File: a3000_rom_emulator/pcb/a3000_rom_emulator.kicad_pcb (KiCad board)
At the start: 4 copper layers, 43.2 x 78.7 mm, 92 parts

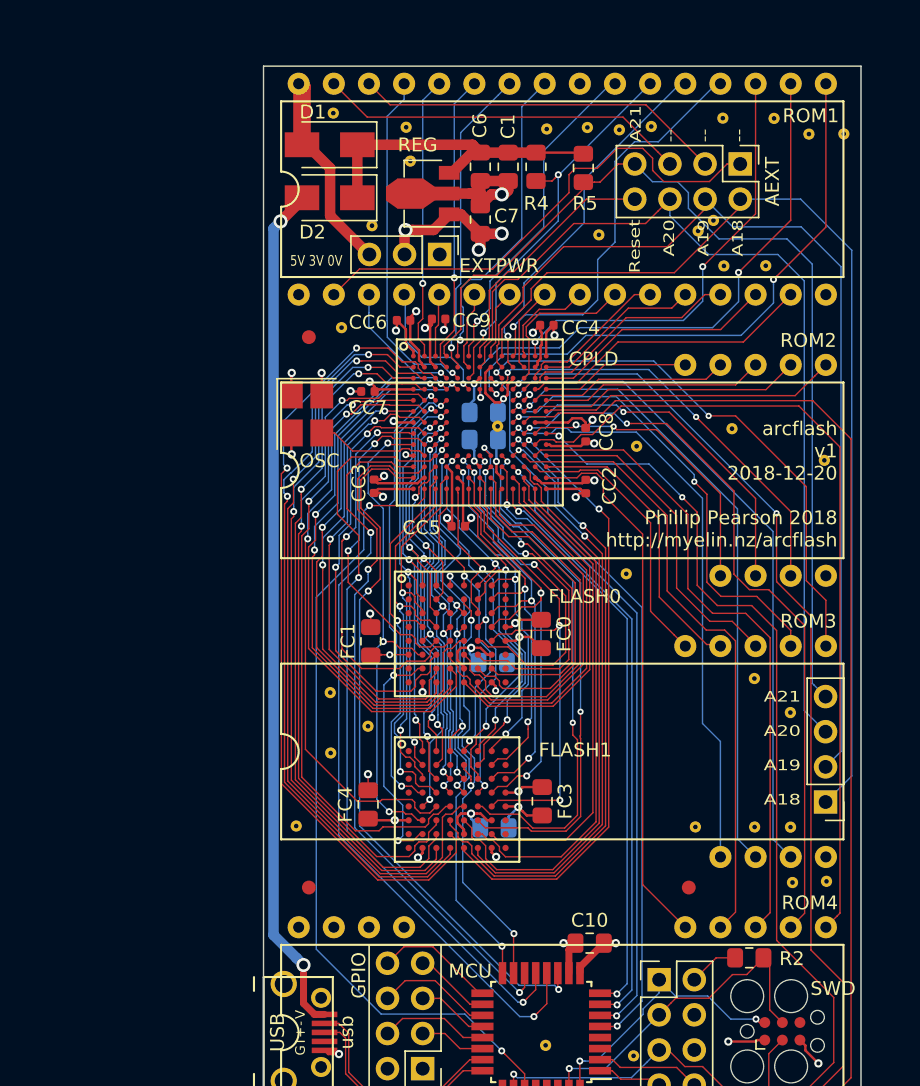
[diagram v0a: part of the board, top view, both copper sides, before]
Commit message: Starting on v2: renamed arc_RESET pin to rom_nOE and added jumper to connect LA21 to rom_A19
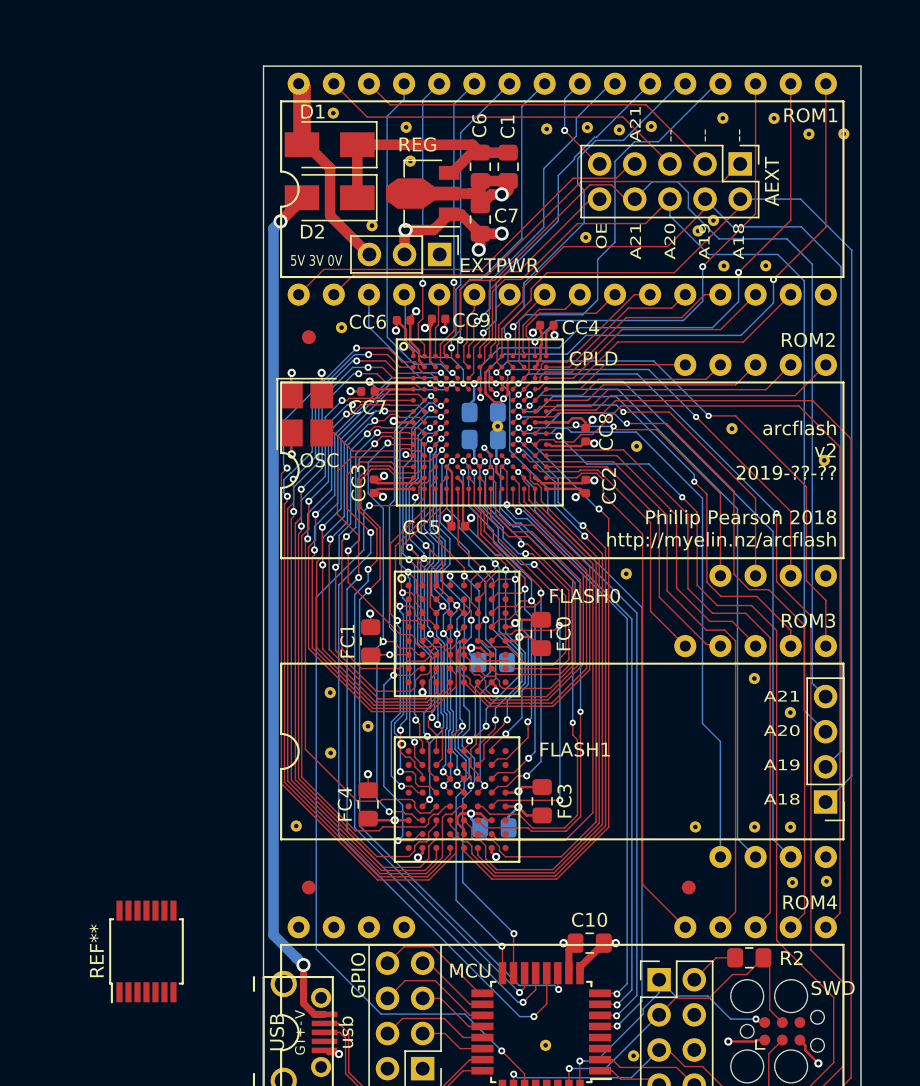
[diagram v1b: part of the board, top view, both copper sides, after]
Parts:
- removed the AEXT at (174.2, 36.3)
- removed R4, R5: 10k, Resistor_SMD:R_0805_2012Metric_Pad1.15x1.40mm_HandSolder
- added AEXT: Extras, Connector_PinHeader_2.54mm:PinHeader_2x05_P2.54mm_Vertical, F.Cu at (174.2, 36.3)
- added REF**: TSSOP-14_4.4x5mm_P0.65mm, Package_SO:TSSOP-14_4.4x5mm_P0.65mm, F.Cu at (131.2, 93.2)
- moved staple_single19 0.97 mm to (163.0, 41.6)
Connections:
- CPLD pad A7: arc_RESET -> rom_nOE
- ROM1 pad 1: (no net) -> rom_A19_ext
- ROM1 pad 24: (no net) -> rom_nOE_ext
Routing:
- net rom_A19_ext: track 0.00 -> 28.2 mm
- net arc_RESET: track 18.3 -> 0.00 mm
- net rom_nOE: track 0.00 -> 15.7 mm
- net rom_nOE_ext: track 0.00 -> 7.37 mm, vias 0 -> 1
- net 5V: track 23.3 -> 17.8 mm
- net rom_A16_ext: track 36.6 -> 33.3 mm
- net rom_nCS: track 28.5 -> 26.8 mm, vias 2 -> 1
- net rom_D7: track 26.4 -> 27.9 mm
- net flash_A19: track 29.2 -> 28.6 mm
- net rom_A19: track 70.2 -> 69.6 mm
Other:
- board text added: "OE A21 A20 A19 A18"
- board text added: "TODO - wire up A21 (rom_A19) to ROM pin 1 - remove pullups for A21 and romcs* - remove osc and add pin + gnd - add power sense voltage divider -> mcu gpio - OR 74lvt125d for: - reset sense - reset drive - power sense - POR drive -> then we can use the CPLD reset pin for RPC OE"
- board text added: "arcflash v2 2019-??-?? Phillip Pearson 2018 http://myelin.nz/arcflash"
- board text removed: "Reset A20 A19 A18"
- board text removed: "arcflash v1 2018-12-20 Phillip Pearson 2018 http://myelin.nz/arcflash"

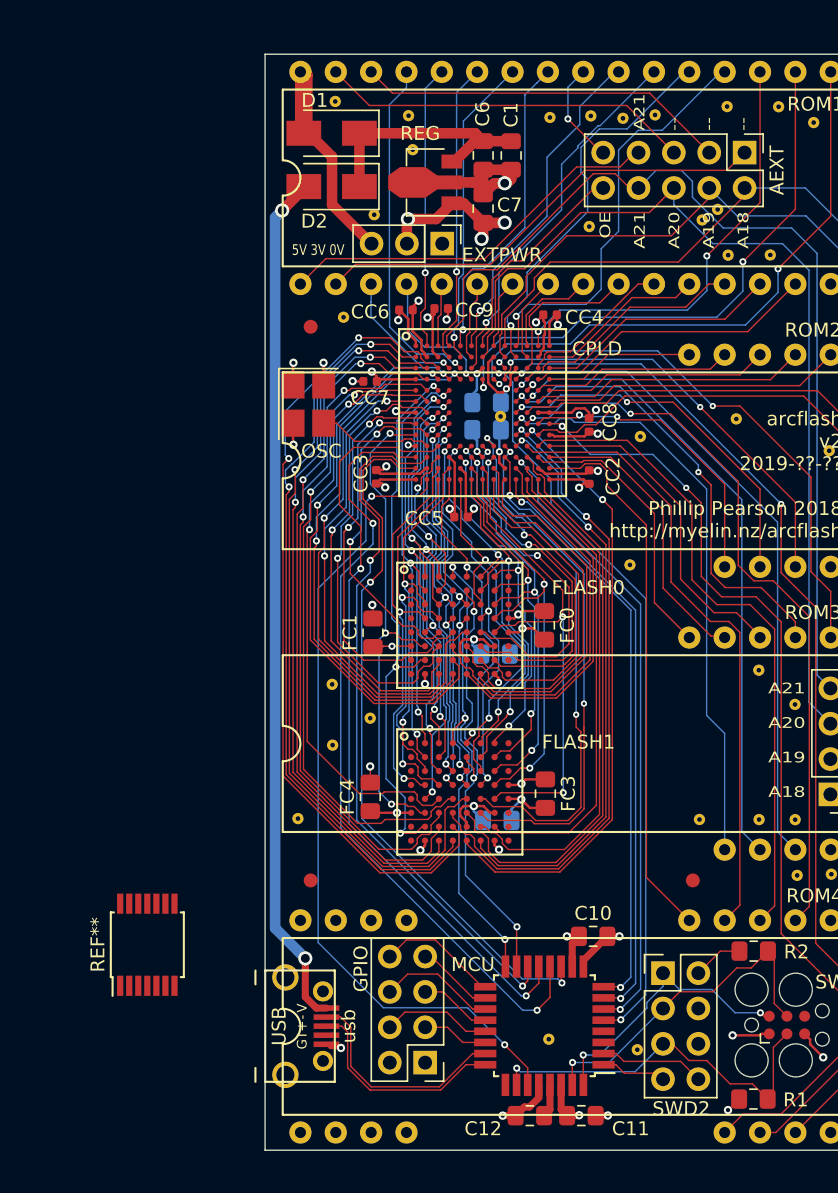
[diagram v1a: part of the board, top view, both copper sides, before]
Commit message: v2: 74lvt125 added and all lines routed, I think
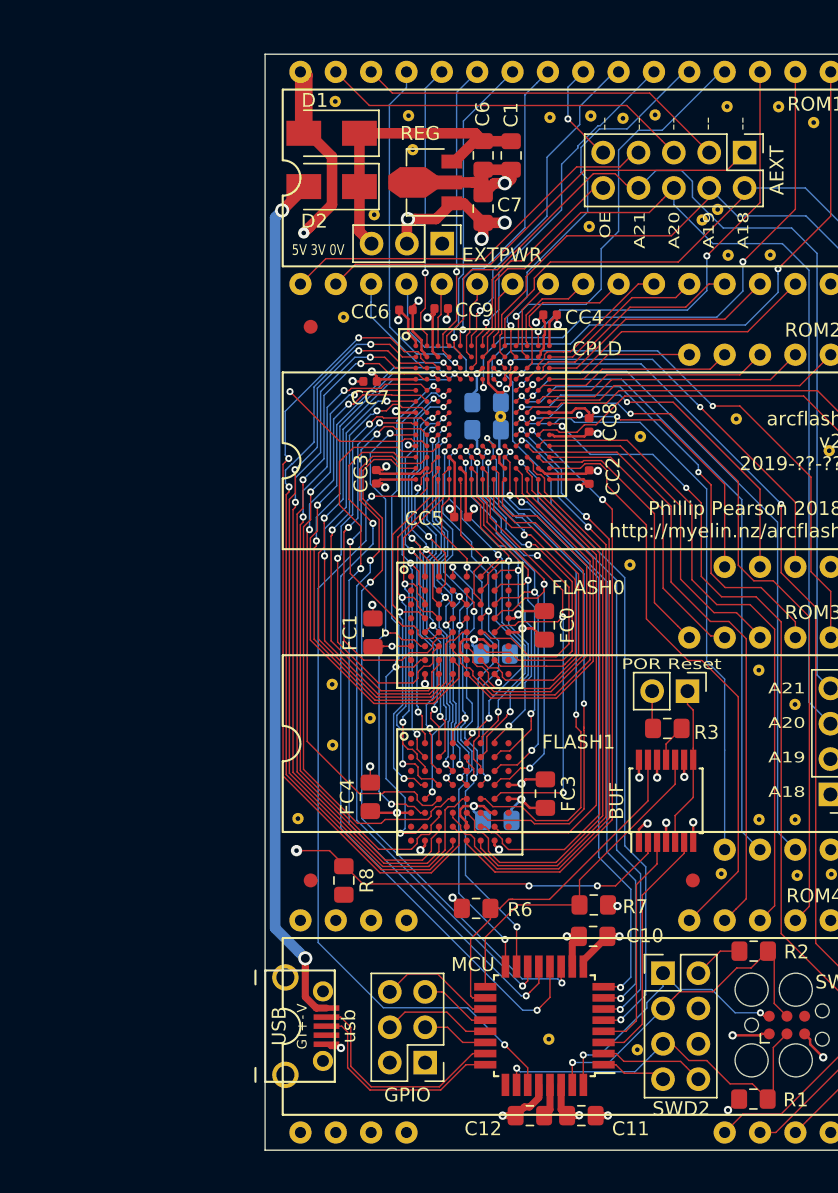
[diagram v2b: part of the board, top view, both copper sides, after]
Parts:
- removed the GPIO at (151.2, 101.7)
- removed OSC: osc, Oscillator:Oscillator_SMD_Abracon_ASE-4Pin_3.2x2.5mm_HandSoldering
- removed REF**: TSSOP-14_4.4x5mm_P0.65mm, Package_SO:TSSOP-14_4.4x5mm_P0.65mm
- added BUF: Reset buffer, Package_SO:TSSOP-14_4.4x5mm_P0.65mm, F.Cu at (168.5, 82.8)
- added GPIO: gpio, Connector_PinHeader_2.54mm:PinHeader_2x03_P2.54mm_Vertical, F.Cu at (151.2, 101.7)
- added R3: 100R, Resistor_SMD:R_0805_2012Metric_Pad1.15x1.40mm_HandSolder, F.Cu at (168.6, 77.7)
- added R6: NF 10k, Resistor_SMD:R_0805_2012Metric_Pad1.15x1.40mm_HandSolder, F.Cu at (154.9, 90.6)
- added R7: NF 10k, Resistor_SMD:R_0805_2012Metric_Pad1.15x1.40mm_HandSolder, F.Cu at (163.3, 90.3)
- added R8: 10k, Resistor_SMD:R_0805_2012Metric_Pad1.15x1.40mm_HandSolder, F.Cu at (145.4, 88.6)
- added RESET: reset/POR, Connector_PinHeader_2.54mm:PinHeader_1x02_P2.54mm_Vertical, F.Cu at (170.1, 75.0)
- moved staple_single30 4.20 mm to (172.5, 88.1)
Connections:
- CPLD pad K2: cpld_clock_osc -> rom_5V
- EXTPWR pad 3: rom_5V -> 5V
- MCU pad 17: mcu_GPIO5 -> ndrive_arc_RESET
- MCU pad 18: mcu_GPIO4 -> ndrive_arc_POR
- MCU pad 3: (no net) -> arc_RESET_buffered
- MCU pad 4: (no net) -> rom_5V_buffered
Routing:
- net rom_5V: track 14.7 -> 100.2 mm, vias 0 -> 5
- net ndrive_arc_POR: track 0.00 -> 25.6 mm
- net ndrive_arc_RESET: track 0.00 -> 24.6 mm
- net arc_RESET_buffered: track 0.00 -> 17.7 mm
- net rom_5V_buffered: track 0.00 -> 16.1 mm
- net arc_RESET: track 0.00 -> 11.5 mm
- net mcu_GPIO5: track 8.74 -> 0.00 mm
- net cpld_clock_osc: track 8.24 -> 0.00 mm
- net mcu_GPIO4: track 5.55 -> 0.00 mm
- net GND: track 80.6 -> 86.0 mm, vias 28 -> 32
- net 5V: track 17.8 -> 22.3 mm
- net rom_D31: track 39.2 -> 42.7 mm
- net arc_POR_R: track 0.00 -> 2.71 mm
- net arc_POR: track 0.00 -> 2.71 mm
- net 3V3: track 87.4 -> 87.3 mm, vias 25 -> 26
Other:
- board text added: "-- -- -- -- --"
- board text added: "POR Reset"
- board text removed: "A21 -- -- --"

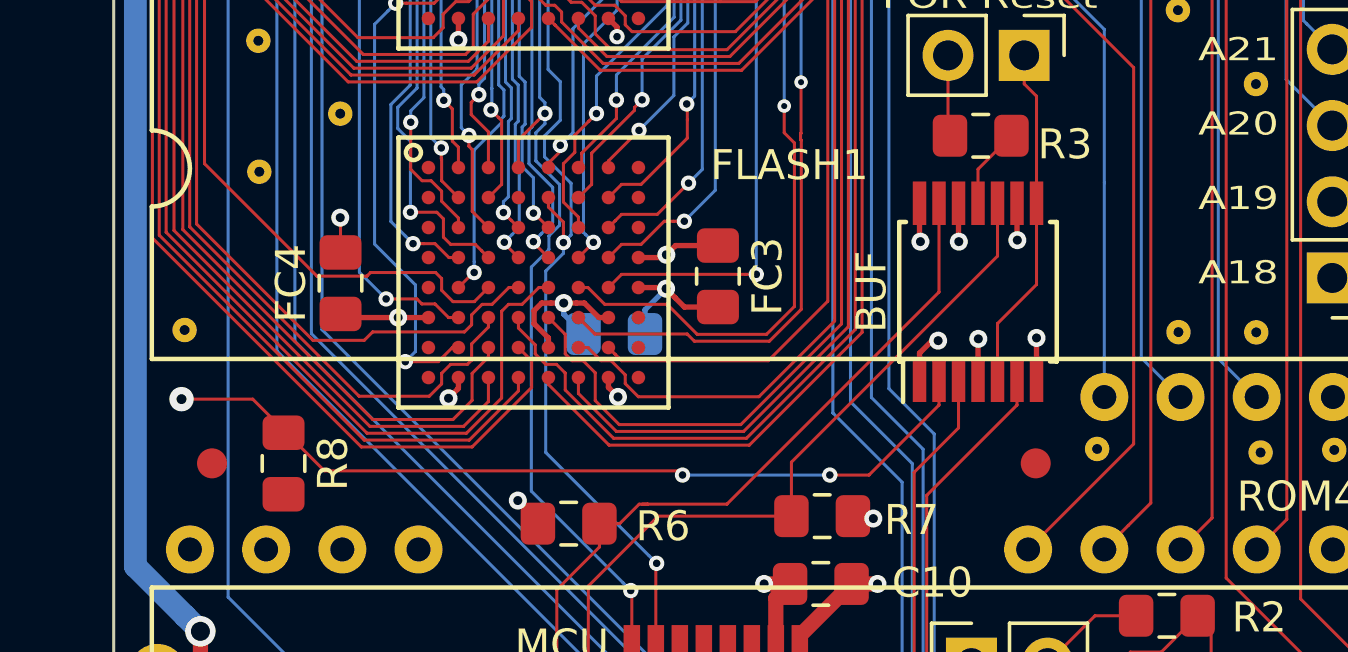
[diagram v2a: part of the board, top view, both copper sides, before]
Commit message: Added decoupling cap for BUF
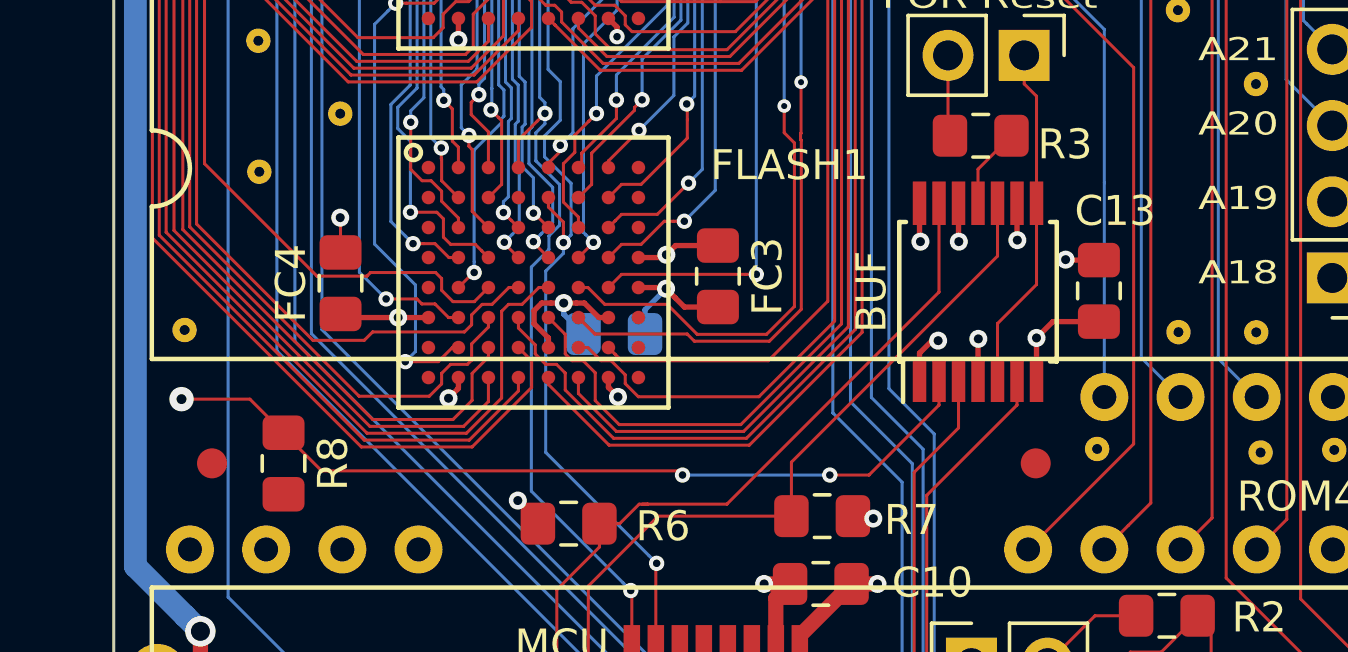
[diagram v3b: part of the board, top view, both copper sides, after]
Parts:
- added C13: 100n, Capacitor_SMD:C_0805_2012Metric_Pad1.15x1.40mm_HandSolder, F.Cu at (172.5, 82.8)
- BUF: value Reset buffer -> 74LVT125PW
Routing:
- net GND: track 86.0 -> 88.3 mm
- net 3V3: track 87.3 -> 88.4 mm, vias 26 -> 27
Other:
- board text added: "TODO - done: wire up A21 (rom_A19) to ROM pin 1 - done: remove pullups for A21 and romcs* - done: remove osc and connect to rom_5V - skipped: add power sense voltage divider -> mcu gpio - done: OR 74lvt125d for: - reset sense - reset drive - power sense - POR drive -> then we can use the CPLD reset pin for RPC OE"
- board text removed: "TODO - wire up A21 (rom_A19) to ROM pin 1 - remove pullups for A21 and romcs* - remove osc and add pin + gnd - add power sense voltage divider -> mcu gpio - OR 74lvt125d for: - reset sense - reset drive - power sense - POR drive -> then we can use the CPLD reset pin for RPC OE"
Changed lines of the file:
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@@
     (thickness 1.6)
     (drawings 14)
-    (tracks 2549)
+    (tracks 2555)
     (zones 0)
-    (modules 95)
+    (modules 96)
     (nets 152)
   )
@@
       (effects (font (size 1 1) (thickness 0.15)))
     )
-    (fp_text value "Reset buffer" (at 0 3.55 90) (layer F.Fab)
+    (fp_text value 74LVT125PW (at 0 3.55 90) (layer F.Fab)
       (effects (font (size 1 1) (thickness 0.15)))
     )
@@
     )
   )
+  (module Capacitor_SMD:C_0805_2012Metric_Pad1.15x1.40mm_HandSolder (layer F.Cu)
+    (at 172.54 82.82 90)
+    (descr "Capacitor SMD 0805 (2012 Metric), square (rectangular) end terminal, IPC_7351 nominal with elongated pad for handsoldering. (Body size source: https://docs.google.com/spreadsheets/d/1BsfQQcO9C6DZCsRaXUlFlo91Tg2WpOkGARC1WS5S8t0/edit?usp=sharing), generated with kicad-footprint-generator")
+    (tags "capacitor handsolder")
+    (attr smd)
+    (fp_text reference C13 (at 2.66 0.54 180) (layer F.SilkS)
+      (effects (font (size 1 1) (thickness 0.15)))
+    )
+    (fp_text value 100n (at 0 1.65 90) (layer F.Fab)
+      (effects (font (size 1 1) (thickness 0.15)))
+    )
+    (fp_line (start -1 0.6) (end -1 -0.6) (layer F.Fab) (width 0.1))
+    (fp_line (start -1 -0.6) (end 1 -0.6) (layer F.Fab) (width 0.1))
+    (fp_line (start 1 -0.6) (end 1 0.6) (layer F.Fab) (width 0.1))
+    (fp_line (start 1 0.6) (end -1 0.6) (layer F.Fab) (width 0.1))
+    (fp_line (start -0.261252 -0.71) (end 0.261252 -0.71) (layer F.SilkS) (width 0.12))
+    (fp_line (start -0.261252 0.71) (end 0.261252 0.71) (layer F.SilkS) (width 0.12))
+    (fp_line (start -1.85 0.95) (end -1.85 -0.95) (layer F.CrtYd) (width 0.05))
+    (fp_line (start -1.85 -0.95) (end 1.85 -0.95) (layer F.CrtYd) (width 0.05))
+    (fp_line (start 1.85 -0.95) (end 1.85 0.95) (layer F.CrtYd) (width 0.05))
+    (fp_line (start 1.85 0.95) (end -1.85 0.95) (layer F.CrtYd) (width 0.05))
+    (fp_text user %R (at 0 0 90) (layer F.Fab)
+      (effects (font (size 0.5 0.5) (thickness 0.08)))
+    )
+    (pad 1 smd roundrect (at -1.025 0 90) (size 1.15 1.4) (layers F.Cu F.Paste F.Mask) (roundrect_rratio 0.217391)
+      (net 27 GND))
+    (pad 2 smd roundrect (at 1.025 0 90) (size 1.15 1.4) (layers F.Cu F.Paste F.Mask) (roundrect_rratio 0.217391)
+      (net 9 3V3))
+    (model ${KISYS3DMOD}/Capacitor_SMD.3dshapes/C_0805_2012Metric.wrl
+      (at (xyz 0 0 0))
+      (scale (xyz 1 1 1))
+      (rotate (xyz 0 0 0))
+    )
+  )
   (gr_text "POR Reset" (at 165.31 73.03) (layer F.SilkS)
     (effects (font (size 0.77 1) (thickness 0.1)) (justify left))
   )
-  (gr_text "TODO\n- wire up A21 (rom_A19) to ROM pin 1\n- remove pullups for A21 and romcs*\n- remove osc and add pin + gnd\n- add power sense voltage divider -> mcu gpio\n- OR 74lvt125d for:\n  - reset sense\n  - reset drive\n  - power sense\n  - POR drive\n  -> then we can use the CPLD reset pin for RPC OE" (at 205.74 40.64) (layer Dwgs.User)
+  (gr_text "TODO\n- done: wire up A21 (rom_A19) to ROM pin 1\n- done: remove pullups for A21 and romcs*\n- done: remove osc and connect to rom_5V\n- skipped: add power sense voltage divider -> mcu gpio\n- done: OR 74lvt125d for:\n  - reset sense\n  - reset drive\n  - power sense\n  - POR drive\n  -> then we can use the CPLD reset pin for RPC OE" (at 205.74 40.64) (layer Dwgs.User)
     (effects (font (size 1 1) (thickness 0.2)) (justify left))
   )
@@
   (segment (start 153.84 90.48) (end 153.17 89.81) (width 0.1778) (layer F.Cu) (net 9))
   (segment (start 153.84 90.58) (end 153.84 90.48) (width 0.1778) (layer F.Cu) (net 9))
+  (via (at 171.43 81.78) (size 0.6) (drill 0.3) (layers F.Cu B.Cu) (net 9))
+  (segment (start 171.445 81.795) (end 171.43 81.78) (width 0.1778) (layer F.Cu) (net 9))
+  (segment (start 172.54 81.795) (end 171.445 81.795) (width 0.1778) (layer F.Cu) (net 9))
   (via (at 154.71 69.25) (size 0.51) (drill 0.25) (layers F.Cu B.Cu) (net 10))
   (segment (start 154.71 68.58867) (end 154.71 69.25) (width 0.1016) (layer F.Cu) (net 10))
@@
   (segment (start 166.56 85.8) (end 166.56 84.8972) (width 0.1778) (layer F.Cu) (net 27))
   (segment (start 166.56 84.8972) (end 166.9772 84.48) (width 0.1778) (layer F.Cu) (net 27))
+  (segment (start 171.005 83.845) (end 170.46 84.39) (width 0.1778) (layer F.Cu) (net 27))
+  (segment (start 172.54 83.845) (end 171.005 83.845) (width 0.1778) (layer F.Cu) (net 27))
   (via (at 148.78 83.09) (size 0.51) (drill 0.25) (layers F.Cu B.Cu) (net 28))
   (segment (start 149.805872 83.09) (end 149.972271 83.256399) (width 0.1016) (layer F.Cu) (net 28))
@@
   (segment (start 158.66 88.96) (end 163.57 88.96) (width 0.1016) (layer B.Cu) (net 132))
   (segment (start 164.8766 88.96) (end 163.57 88.96) (width 0.1016) (layer F.Cu) (net 132))
-  (segment (start 144.335 86.43) (end 141.96 86.43) (width 0.1016) (layer F.Cu) (net 132))
-  (segment (start 146.725 88.82) (end 144.335 86.43) (width 0.1016) (layer F.Cu) (net 132))
-  (segment (start 158.52 88.82) (end 146.725 88.82) (width 0.1016) (layer F.Cu) (net 132))
+  (segment (start 144.24 86.43) (end 141.96 86.43) (width 0.1016) (layer F.Cu) (net 132))
+  (segment (start 145.36 87.55) (end 144.24 86.43) (width 0.1016) (layer F.Cu) (net 132))
+  (segment (start 146.63 88.82) (end 145.36 87.55) (width 0.1016) (layer F.Cu) (net 132))
+  (segment (start 158.52 88.82) (end 146.63 88.82) (width 0.1016) (layer F.Cu) (net 132))
   (segment (start 158.66 88.96) (end 158.52 88.82) (width 0.1016) (layer F.Cu) (net 132))
   (via (at 161.02838 95.9358) (size 0.51) (drill 0.25) (layers F.Cu B.Cu) (net 133))

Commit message: Added 1 and > graphics to make assembly easier
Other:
- board text added: "1"
- board text added: ">"
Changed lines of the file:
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@@
   (general
     (thickness 1.6)
-    (drawings 14)
+    (drawings 20)
     (tracks 2555)
     (zones 0)
@@
     )
   )
+  (gr_text > (at 144.52 38.72) (layer F.SilkS)
+    (effects (font (size 0.762 0.762) (thickness 0.1524)))
+  )
+  (gr_text > (at 144.48 34.73) (layer F.SilkS)
+    (effects (font (size 0.762 0.762) (thickness 0.1524)))
+  )
+  (gr_text 1 (at 166.38 94.8) (layer F.SilkS)
+    (effects (font (size 0.762 0.762) (thickness 0.1524)))
+  )
+  (gr_text 1 (at 153.23 101.54) (layer F.SilkS)
+    (effects (font (size 0.762 0.762) (thickness 0.1524)))
+  )
+  (gr_text 1 (at 164.1 103.02 90) (layer F.SilkS)
+    (effects (font (size 0.762 0.762) (thickness 0.1524)))
+  )
+  (gr_text 1 (at 165.32 85.94) (layer F.SilkS)
+    (effects (font (size 0.762 0.762) (thickness 0.1524)))
+  )
   (gr_text "POR Reset" (at 165.31 73.03) (layer F.SilkS)
